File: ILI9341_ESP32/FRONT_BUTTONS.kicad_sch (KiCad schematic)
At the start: 23 parts, among them J5 Micro_SD_Card_CD, J6 Conn_01x18_Socket, Q2 BC817, SW10 SW_Push, SW11 SW_Push, SW12 SW_Push, SW2 SW_Push, SW3 SW_Push, SW4 SW_Push, SW5 SW_Push, SW9 SW_Push, U8 IPCB05501F20S3V, U9 IPCB05501M20S3V

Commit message: zwischenstand v2
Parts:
- added C12, C13: 100n, Capacitor_SMD:C_1206_3216Metric, symbol Device:C
- added C14, C17, C18, C6, C7: 4µ7, Capacitor_SMD:C_1206_3216Metric, symbol Device:C
- added C15, C16: 220p, Capacitor_SMD:C_0603_1608Metric, symbol Device:C
- added C5: 470µ, Capacitor_Tantalum_SMD:CP_EIA-7343-43_Kemet-X, symbol Device:C_Polarized
- added D1: LED, LED_SMD:LED_0603_1608Metric, symbol Device:LED
- added FB1, FB2, FB3: FerriteBead_Small, Inductor_SMD:L_0805_2012Metric, symbol Device:FerriteBead_Small
- added Q3, Q7: Q_PMOS_GSD, Package_TO_SOT_SMD:SOT-323_SC-70, symbol Device:Q_PMOS_GSD
- added Q8: BC817, Package_TO_SOT_SMD:SOT-323_SC-70, symbol Transistor_BJT:BC817
- added R1, R2, R39, R40: 5K1, Resistor_SMD:R_0603_1608Metric, symbol Device:R
- added R10, R11, R14, R16, R17, R18, R19, R20, R21, R22, R32, R37, R38: 5K1, Resistor_SMD:R_0603_1608Metric_Pad0.98x0.95mm_HandSolder, symbol Device:R
- added R3, R35, R36, R8: 100K, Resistor_SMD:R_0603_1608Metric_Pad0.98x0.95mm_HandSolder, symbol Device:R
- added U11: CS-1193SDIG-2X7SMT(H4.3), TheBrutzlers_Lib:PM200-2-07-S-4.3, symbol easyeda2kicad:CS-1193SDIG-2X7SMT(H4.3)
- added U3: ESP32-WROVER-E-N8R8, easyeda2kicad:WIFI-SMD_ESP32-WROVER-IE8MB, symbol easyeda2kicad:ESP32-WROVER-E-N8R8
- added U4: PAM8406D, Package_SO:SOP-16_3.9x9.9mm_P1.27mm, symbol Amplifier_Audio:PAM8406D
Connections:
- net CLK: now also U3.30 (IO18); no longer U9.14
- net KEY_A: now also SW11.2, U3.8 (IO32); no longer U8.14
- net KEY_B: now also SW12.2, U3.9 (IO33); no longer U8.16
- net KEY_DOWN: now also SW5.2, R32.2; no longer U8.13
- net KEY_LEFT: now also SW3.2, R37.1, R38.1, U3.6 (IO34); no longer U8.19
- net KEY_RIGHT: now also SW2.2, R38.2; no longer U8.15
- net KEY_SELECT: now also SW10.2, U3.12 (IO27); no longer U8.20
- net KEY_START: now also SW9.2, R14.1, U3.5 (SENSOR_VN); no longer U8.18
- net KEY_UP: now also SW4.2, R21.1, R32.1, U3.7 (IO35); no longer U8.17
- net LCD_BCKL: now also U3.13 (IO14); no longer U9.10
- net LCD_DC: now also U3.33 (IO21); no longer U9.11
- net LCD_~{CS}: now also R18.1, U3.29 (IO5); no longer U9.12
- net MOSI: now also U3.37 (IO23); no longer U9.15
- net SD_MISO: now also R22.1, U3.31 (IO19); no longer U9.16
- net SD_~{CS}: now also U3.36 (IO22); no longer U9.13
- net SPK+: now also Q7.3 (D); no longer U9.20
- net SPK-: now also Q3.3 (D); no longer U9.19
- net 3V3 renamed +3V3
- net +3V3: now also FB1.1, R10.2, R11.2, R14.2, R16.2, R17.2, R18.2, R39.1, R40.1, U11.4, U3.2 (3V3); no longer U9.18
- net A: no longer names the net of U9.8
- net A: no longer SW11.2
- net B: no longer names the net of U9.6
- net B: no longer SW12.2
- net DOWN: no longer names the net of U9.7
- net DOWN: no longer SW5.2
- net FRONT_3V3: no longer names the net of U8.4
- net FRONT_CLK: no longer names the net of U8.8
- net FRONT_GND: no longer names the net of U8.11
- net FRONT_GND: no longer U8.3
- net FRONT_LCD_BCLK: no longer names the net of U8.12
- net FRONT_LCD_DC: no longer names the net of U8.9
- net FRONT_LCD_~{CS}: no longer names the net of U8.10
- net FRONT_MOSI: no longer names the net of U8.5
- net FRONT_SD_MISO: no longer names the net of U8.6
- net FRONT_SD_~{CS}: no longer names the net of U8.7
- net FRONT_SPK+: no longer names the net of U8.2
- net FRONT_SPK-: no longer names the net of U8.1
- net F_GND renamed GND
- net GND: now also C14.2, C15.2, C16.1, C5.2, C6.2, C7.2, Q8.2 (E), R19.2, R2.2, R20.2, R21.2, R22.2, R36.2, R37.2, U11.3, U3.1 (GND), U3.15 (GND), U3.38 (GND), U3.39 (GND), U4.11 (GND), U4.15 (PGNDR), U4.2 (PGNDL); no longer U9.17, U9.9
- net LEFT: no longer names the net of U9.1
- net LEFT: no longer SW3.2
- net RIGHT: no longer names the net of U9.5
- net RIGHT: no longer SW2.2
- net SELECT: no longer names the net of U9.2
- net SELECT: no longer SW10.2
- net START: no longer names the net of U9.4
- net START: no longer SW9.2
- net UP: no longer names the net of U9.3
- net UP: no longer SW4.2
- new net: C5.1, C6.1, C7.1, FB1.2, R1.1, U4.12 (~{SHND}), U4.13 (PVDDR), U4.4 (PVDDL), U4.5 (~{MUTE}), U4.6 (VDD)
- new net: FB2.1, U4.1 (+OUT_L)
- new net: C16.2, C17.1, FB2.2
- new net: C15.1, C18.1, FB3.2
- new net: C12.2, R3.1
- new net: R3.2, U4.7 (INL)
- new net: Q3.1 (G), Q7.1 (G), Q8.3 (C), R39.2
- new net: D1.1 (K), R20.1
- new net: R1.2, R2.1, U4.9 (MODE)
- new net: C13.2, R8.1
- new net: R8.2, U4.10 (INR)
- new net: C14.1, U4.8 (VREF)
- new net: FB3.1, U4.16 (+OUT_R)
- new net AudioLEFT: C17.2, Q3.2 (S), U11.13
- new net AudioRIGHT: C18.2, Q7.2 (S), U11.14
- new net EN: R16.1, U11.8, U3.3 (EN)
- new net I2C_CLK: R10.1, U11.1, U3.26 (IO4)
- new net I2C_SDA: R11.1, U11.2, U3.23 (IO15)
- new net KEY_MENU: U11.9, U3.16 (IO13)
- new net KEY_OPTION: R17.1, U11.10, U3.25 (IO0)
- new net LED: D1.2 (A), R19.1, U11.6, U3.24 (IO2)
- new net RXD: U11.5, U3.34 (RXD0)
- new net SOUND_LEFT: C12.1, U3.11 (IO26)
- new net SOUND_RIGHT: C13.1, U3.10 (IO25)
- new net SPK_~{EN}: Q8.1 (B), R40.2, U11.12
- new net TXD: U11.7, U3.35 (TXD0)
- new net V_BATT: R35.1, U11.11
- new net V_BAT_ADC: R35.2, R36.1, U3.4 (SENSOR_VP)
- no-connect marks 3 -> 15
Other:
- note added: "FOOTPRINT POSSITION FINDEN"
- note added: "SPEAKER ENABLE TESTEN"
- moved on the sheet: C20, C26, C9, J5, J6, LS1, Q2, R23, R26, R27, R28, R45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

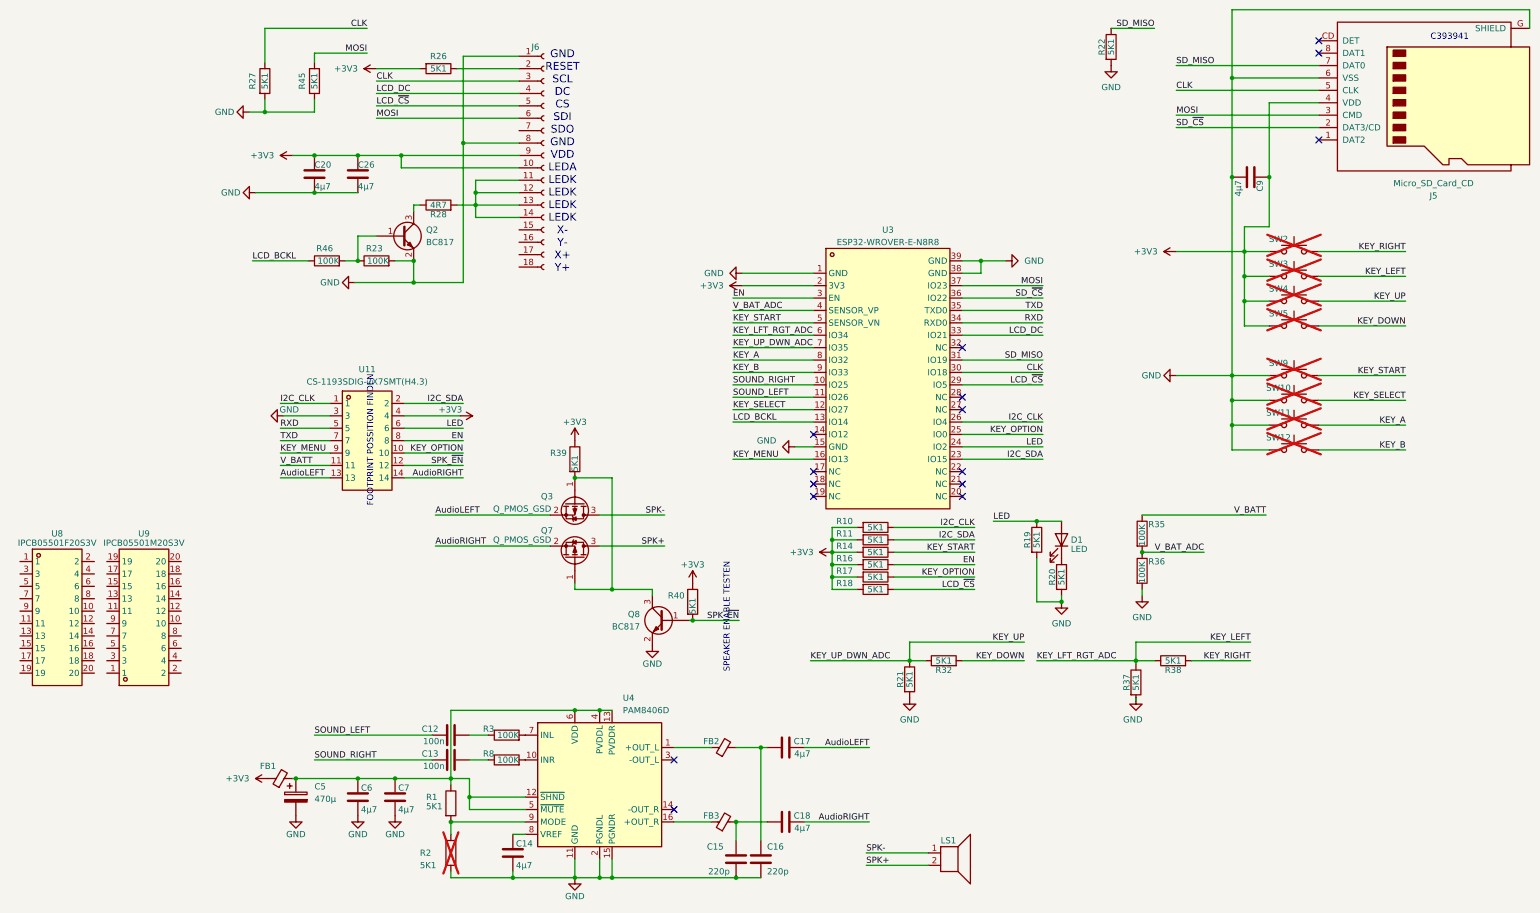
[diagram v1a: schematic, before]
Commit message: Update PCB and add RGB
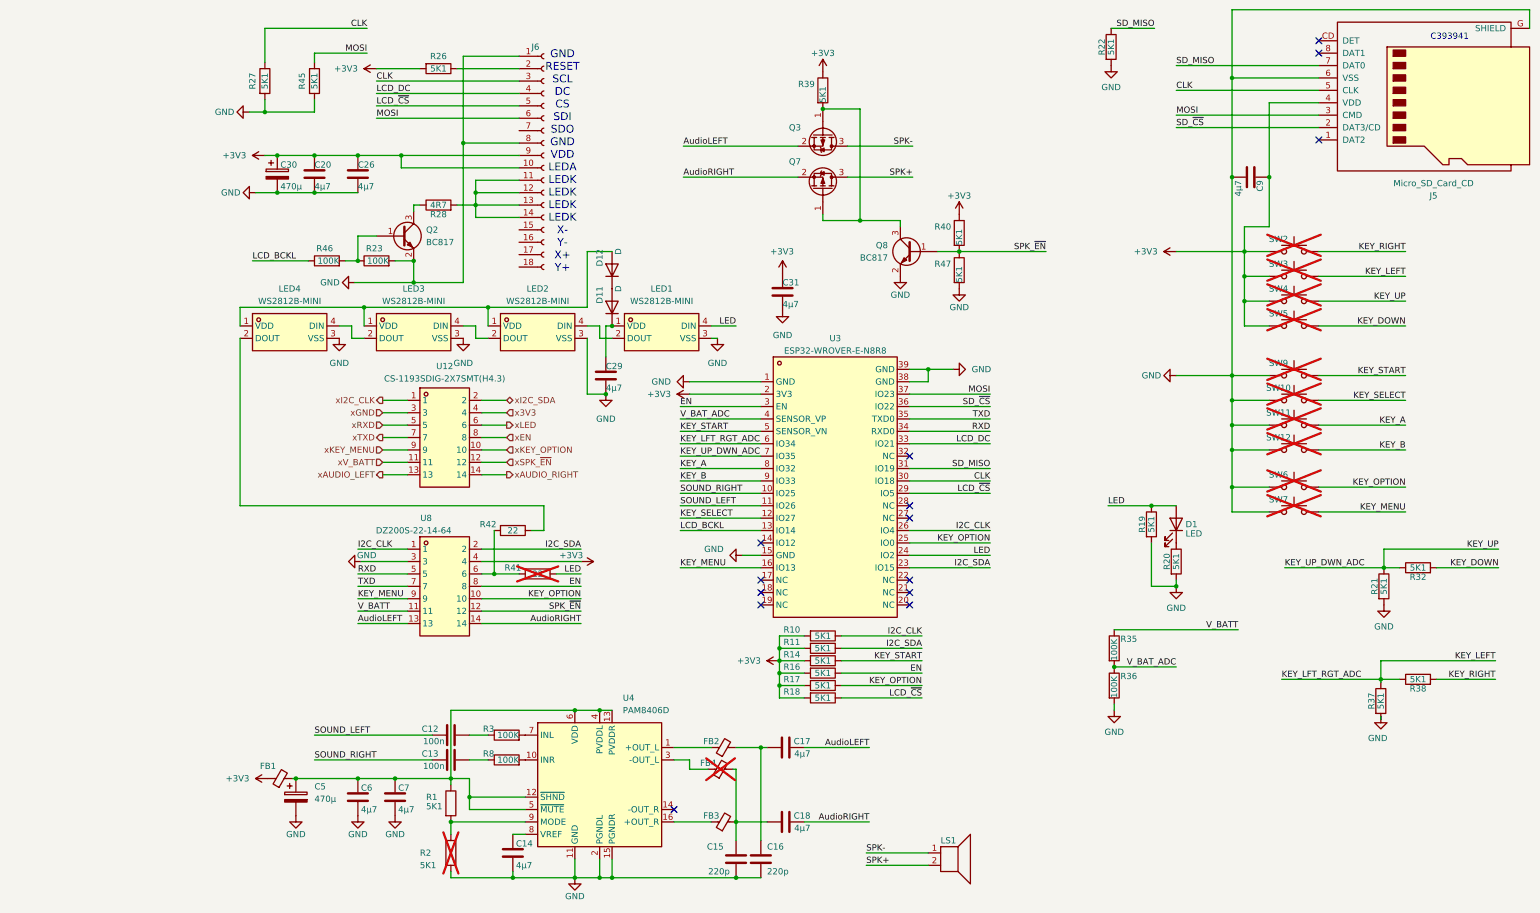
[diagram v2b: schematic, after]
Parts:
- removed U11: CS-1193SDIG-2X7SMT(H4.3), TheBrutzlers_Lib:PM200-2-07-S-4.3, symbol easyeda2kicad:CS-1193SDIG-2X7SMT(H4.3)
- removed U8: IPCB05501F20S3V, easyeda2kicad:CONN-SMD_20P-P0.50_INCP_IPCB05501F20S3V, symbol easyeda2kicad:IPCB05501F20S3V
- removed U9: IPCB05501M20S3V, easyeda2kicad:CONN-SMD_20P-P0.50_INCP_IPCB05501M20S3V, symbol easyeda2kicad:IPCB05501M20S3V
- added C29, C31: 4µ7, Capacitor_SMD:C_1206_3216Metric, symbol Device:C
- added C30: 470µ, Capacitor_Tantalum_SMD:CP_EIA-7343-43_Kemet-X, symbol Device:C_Polarized
- added D11, D12: D, Diode_SMD:Nexperia_CFP3_SOD-123W, symbol Device:D
- added FB4: FerriteBead_Small, Inductor_SMD:L_0805_2012Metric, symbol Device:FerriteBead_Small
- added LED1, LED2, LED3, LED4: WS2812B-MINI, easyeda2kicad:LED-SMD_4P-L3.5-W3.5-TL_WS2812B, symbol easyeda2kicad:WS2812B-MINI
- added R41, R42: 22, Resistor_SMD:R_0603_1608Metric_Pad0.98x0.95mm_HandSolder, symbol Device:R
- added R47: 5K1, Resistor_SMD:R_0603_1608Metric, symbol Device:R
- added SW6, SW7: SW_Push, TheBrutzlers_Lib:RubberpadButton_250µ_250µ, symbol Switch:SW_Push
- added U12: CS-1193SDIG-2X7SMT(H4.3), TheBrutzlers_Lib:PM200-2-07-S-4.3, symbol easyeda2kicad:CS-1193SDIG-2X7SMT(H4.3)
- added U8: DZ200S-22-14-64, easyeda2kicad:HDR-SMD_14P-P2.00-V-M-R2-C7-LS6.4, symbol easyeda2kicad:DZ200S-22-14-64
- C12, C13: footprint Capacitor_SMD:C_1206_3216Metric -> Capacitor_SMD:C_0603_1608Metric; LCSC C464972 -> (none)
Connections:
- net +3V3: now also C30.1, C31.1, U8.4
- net AudioLEFT: now also U8.13
- net AudioRIGHT: now also U8.14
- net EN: now also U8.8
- net GND: now also C29.2, C30.2, C31.2, LED1.3 (VSS), LED2.3 (VSS), LED3.3 (VSS), LED4.3 (VSS), R47.2, SW6.1, SW7.1, U8.3
- net I2C_CLK: now also U8.1
- net I2C_SDA: now also U8.2
- net KEY_MENU: now also SW7.2, U8.9
- net KEY_OPTION: now also SW6.2, U8.10
- net LED: now also LED1.4 (DIN), R41.1
- net RXD: now also U8.5
- net SPK_~{EN}: now also R47.1, U8.12
- net TXD: now also U8.7
- net V_BATT: now also U8.11
- net at C15.1, C18.1, FB3.2: now also FB4.2
- net at U4.3 (-OUT_L): now also FB4.1
- new net: C29.1, D11.1 (K), LED1.1 (VDD)
- new net: D11.2 (A), D12.1 (K)
- new net: R41.2, R42.2, U8.6
- new net: LED4.2 (DOUT), R42.1
- new net: D12.2 (A), LED2.1 (VDD), LED3.1 (VDD), LED4.1 (VDD)
- new net: LED2.2 (DOUT), LED3.4 (DIN)
- new net: LED1.2 (DOUT), LED2.4 (DIN)
- new net: LED3.2 (DOUT), LED4.4 (DIN)
- new net x3V3: U12.4
- new net xAUDIO_LEFT: U12.13
- new net xAUDIO_RIGHT: U12.14
- new net xEN: U12.8
- new net xGND: U12.3
- new net xI2C_CLK: U12.1
- new net xI2C_SDA: U12.2
- new net xKEY_MENU: U12.9
- new net xKEY_OPTION: U12.10
- new net xLED: U12.6
- new net xRXD: U12.5
- new net xSPK_~{EN}: U12.12
- new net xTXD: U12.7
- new net xV_BATT: U12.11
- no-connect marks 15 -> 14
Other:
- note removed: "FOOTPRINT POSSITION FINDEN"
- note removed: "SPEAKER ENABLE TESTEN"
- moved on the sheet: D1, Q3, Q7, Q8, R10, R11, R14, R16, R17, R18, R19, R20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

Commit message: update nimh charger and battery protection
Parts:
- LED1, LED2, LED3, LED4: LCSC (none) -> C527089; LCSC Part C527089 -> (none)
- U12: LCSC (none) -> C3975171; LCSC Part C3975171 -> (none)
- U3: LCSC (none) -> C2973667; LCSC Part C2973667 -> (none)
- U8: LCSC (none) -> C5160772; LCSC Part C5160772 -> (none)
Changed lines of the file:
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@@
 			)
 		)
-		(property "LCSC Part" "C2973667"
+		(property "LCSC Part" ""
 			(at 140.97 146.05 0)
 			(effects
@@
 			)
 		)
+		(property "LCSC" "C2973667"
+			(at 140.97 111.76 0)
+			(effects
+				(font
+					(size 1.27 1.27)
+				)
+				(hide yes)
+			)
+		)
 		(pin "33"
 		)
@@
 			)
 		)
-		(property "LCSC Part" "C5160772"
+		(property "LCSC Part" ""
 			(at 60.96 149.86 0)
 			(effects
@@
 			)
 		)
+		(property "LCSC" "C5160772"
+			(at 60.96 132.08 0)
+			(effects
+				(font
+					(size 1.27 1.27)
+				)
+				(hide yes)
+			)
+		)
 		(pin "4"
 		)
@@
 			)
 		)
-		(property "LCSC Part" "C3975171"
+		(property "LCSC Part" ""
 			(at 60.96 119.38 0)
 			(effects
@@
 			)
 		)
+		(property "LCSC" "C3975171"
+			(at 60.96 101.6 0)
+			(effects
+				(font
+					(size 1.27 1.27)
+				)
+				(hide yes)
+			)
+		)
 		(pin "1"
 		)
@@
 			)
 		)
-		(property "LCSC Part" "C527089"
+		(property "LCSC Part" ""
 			(at 80.01 93.98 0)
 			(effects
@@
 			)
 		)
+		(property "LCSC" "C527089"
+			(at 80.01 80.01 0)
+			(effects
+				(font
+					(size 1.27 1.27)
+				)
+				(hide yes)
+			)
+		)
 		(pin "2"
 		)
@@
 			)
 		)
-		(property "LCSC Part" "C527089"
+		(property "LCSC Part" ""
 			(at 54.61 93.98 0)
 			(effects
@@
 			)
 		)
+		(property "LCSC" "C527089"
+			(at 54.61 80.01 0)
+			(effects
+				(font
+					(size 1.27 1.27)
+				)
+				(hide yes)
+			)
+		)
 		(pin "2"
 		)
@@
 			)
 		)
-		(property "LCSC Part" "C527089"
+		(property "LCSC Part" ""
 			(at 105.41 93.98 0)
 			(effects
@@
 			)
 		)
+		(property "LCSC" "C527089"
+			(at 105.41 80.01 0)
+			(effects
+				(font
+					(size 1.27 1.27)
+				)
+				(hide yes)
+			)
+		)
 		(pin "2"
 		)
@@
 			)
 		)
-		(property "LCSC Part" "C527089"
+		(property "LCSC Part" ""
 			(at 29.21 93.98 0)
 			(effects
 				(font
+					(size 1.27 1.27)
+				)
+				(hide yes)
+			)
+		)
+		(property "LCSC" "C527089"
+			(at 29.21 80.01 0)
+			(effects
+				(font

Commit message: ordered Version
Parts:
- added R56: 5K1, Resistor_SMD:R_0603_1608Metric, symbol Device:R
- C12, C13, C14, C15, C16, C17, C18, C20, C26, C29, C31, C6, C7, C9, D1, D11, D12, FB1, FB2, FB3, FB4, J5, LS1, Q2, Q8, R1, R39, R40, R47, U3, U4: SOURCED jop -> (none)
- C30, C5, U12, U8: SOURCED (none) -> card
- J6: SOURCED party (2 missing) -> (none)
- Q3, Q7: value Q_PMOS_GSD -> PMOS; SOURCED jop -> (none)
- R10, R11, R14, R16, R17, R18, R19, R20, R21, R22, R23, R26, R27, R28, R3, R32, R35, R36, R37, R38, R41, R42, R45, R46, R8: footprint Resistor_SMD:R_0603_1608Metric_Pad0.98x0.95mm_HandSolder -> Resistor_SMD:R_0603_1608Metric; SOURCED jop -> (none)
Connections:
- net GND: now also R56.1
- net at U3.14 (IO12): now also R56.2
- no-connect marks 14 -> 13

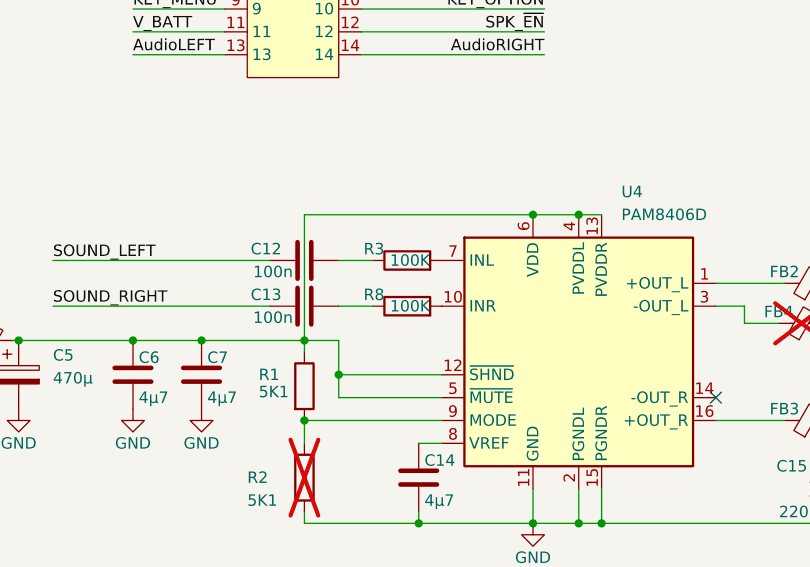
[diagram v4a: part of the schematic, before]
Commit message: upload new untested version
the boosconverter should work now :)
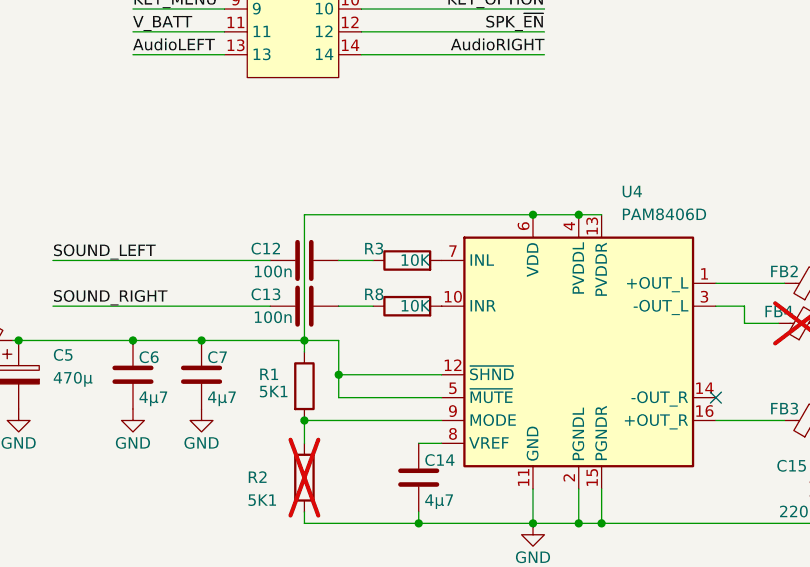
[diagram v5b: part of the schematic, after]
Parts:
- R3, R8: value 100K -> 10K; LCSC C15458 -> C25804
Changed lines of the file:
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@@
 			)
 		)
-		(property "Value" "100K"
+		(property "Value" "10K"
 			(at 76.2 162.56 90)
 			(effects
@@
 			)
 		)
-		(property "LCSC" "C15458"
+		(property "LCSC" "C25804"
 			(at 73.66 162.56 0)
 			(effects
@@
 			)
 		)
-		(property "Value" "100K"
+		(property "Value" "10K"
 			(at 76.2 167.64 90)
 			(effects
@@
 			)
 		)
-		(property "LCSC" "C15458"
+		(property "LCSC" "C25804"
 			(at 73.66 167.64 0)
 			(effects
